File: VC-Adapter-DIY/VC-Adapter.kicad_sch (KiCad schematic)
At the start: 3 parts, among them J1 gba_linkport, U1 XIAO_ESP32_S3, U2 BOB-12009

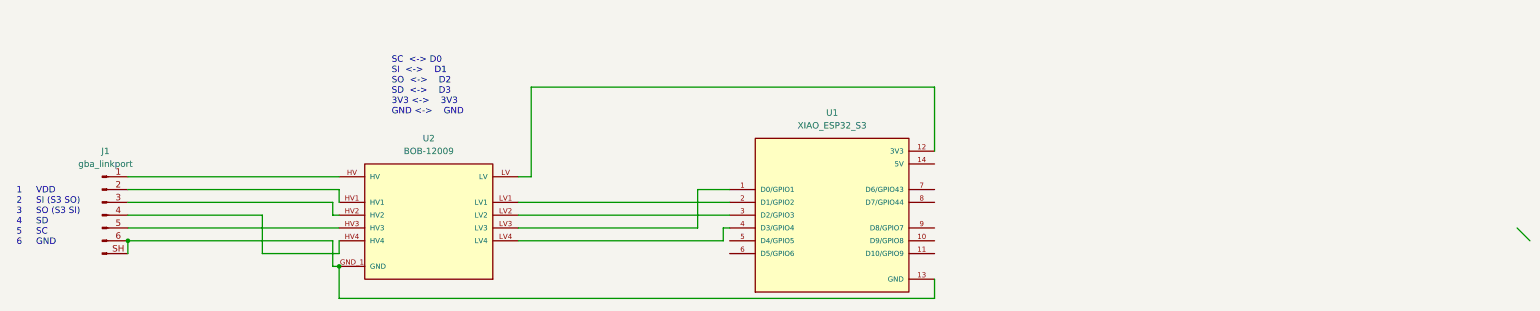
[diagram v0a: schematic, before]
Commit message: Added voltage divider and battery EN support
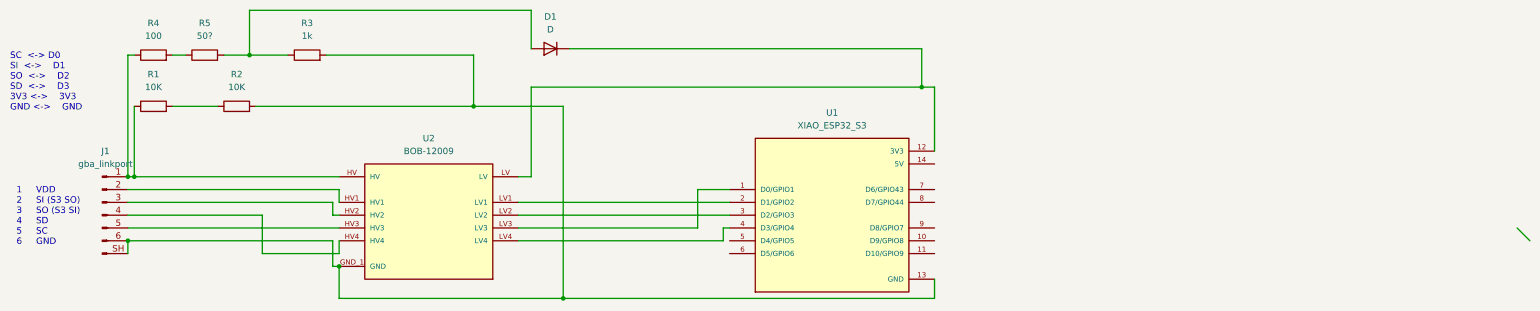
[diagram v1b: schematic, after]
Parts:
- added D1: D, Diode_THT:D_A-405_P7.62mm_Horizontal, symbol Device:D
- added R1, R2: 10K, Resistor_THT:R_Axial_DIN0204_L3.6mm_D1.6mm_P5.08mm_Horizontal, symbol Device:R
- added R3: 1k, Resistor_THT:R_Axial_DIN0204_L3.6mm_D1.6mm_P5.08mm_Horizontal, symbol Device:R
- added R4: 100, Resistor_THT:R_Axial_DIN0204_L3.6mm_D1.6mm_P5.08mm_Horizontal, symbol Device:R
- added R5: 50?, Resistor_THT:R_Axial_DIN0204_L3.6mm_D1.6mm_P5.08mm_Horizontal, symbol Device:R
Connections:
- net GND: now also R2.2, R3.2
- net at J1.1 (Pin_1), U2.HV: now also R1.1, R4.1
- net at U1.12 (3V3), U2.LV: now also D1.1 (K)
- new net: D1.2 (A), R3.1, R5.2
- new net: R4.2, R5.1
- new net: R1.2, R2.1
